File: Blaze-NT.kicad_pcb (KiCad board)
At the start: 2 copper layers, 44.4 x 44.7 mm, 67 parts, among them J1 Micro_SD_Card, J2 TC2030-NL, J3 USB_C_Receptacle, J4 ARM, J5 BATTERY, SW1 SW_SPST, SW2 SW_SPST, U1 W25Q128JVS, U2 STM32F411CEUx, U3 USBLC6-2SC6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

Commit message: Silk updates
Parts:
- added J6: Stemma, Connector_JST:JST_SH_SM04B-SRSS-TB_1x04-1MP_P1.00mm_Horizontal, F.Cu at (130.7, 114.2)
- added R16: 5.1k, Resistor_SMD:R_0603_1608Metric, F.Cu at (134.8, 112.7)
- added R17: 5.1k, Resistor_SMD:R_0603_1608Metric, F.Cu at (134.8, 115.7)
- moved SW2 44.7 mm to (147.2, 92.9)
- moved H4 43.1 mm to (131.0, 121.6)
- moved C2 43.1 mm to (150.3, 105.8)
- moved C3 43.1 mm to (148.7, 105.8)
- moved C6 43.1 mm to (142.6, 94.7)
- moved H1 43.1 mm to (131.0, 84.0)
- moved U4 43.1 mm to (149.5, 119.3)
- moved Y2 43.1 mm to (144.9, 105.6)
- moved AE1 43.1 mm to (156.4, 123.1)
- moved C10 43.1 mm to (159.4, 97.2)
- moved C11 43.1 mm to (157.9, 97.2)
- moved C12 43.1 mm to (152.5, 98.0)
- moved C15 43.1 mm to (163.7, 120.3)
- moved C16 43.1 mm to (162.2, 120.3)
- moved C24 43.1 mm to (152.5, 99.5)
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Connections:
- U2 pad 42: unconnected-(U2-PB6-Pad42) -> /Microcontroller/SCL
- U2 pad 43: unconnected-(U2-PB7-Pad43) -> /Microcontroller/SDA
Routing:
- net /Microcontroller/SCL: track 0.00 -> 27.3 mm, vias 0 -> 2
- net /Microcontroller/SDA: track 0.00 -> 26.9 mm, vias 0 -> 2
- net /Microcontroller/BOOT0: track 25.7 -> 14.9 mm, vias 0 -> 3
- net +5V: track 52.9 -> 57.7 mm
- net /Microcontroller/nRST: track 50.0 -> 53.4 mm
- net /Power Managment/VBATT_Sense/VBATT_IN: track 5.76 -> 7.92 mm
- net +3V3: track 194.5 -> 196.3 mm, vias 5 -> 6
- net Net-(J4-Pin_1): track 34.0 -> 35.5 mm
- net GND: track 0.00 -> 1.46 mm, vias 0 -> 64
- net /Microcontroller/SWD: track 19.8 -> 19.0 mm
- net Net-(D3-A): track 18.2 -> 17.5 mm
- net /MISO: track 108.6 -> 109.3 mm
- net /MOSI: track 111.6 -> 111.0 mm
- net Net-(U4-SW-Pad4): vias 0 -> 7
- net (no net): vias 0 -> 1
- added copper zone on B.Cu, net Net-(U4-SW-Pad4)

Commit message: Addeed part numbers
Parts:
- added D5: LED, LED_SMD:LED_0603_1608Metric, F.Cu at (145.9, 114.5)
- added G***: LOGO, Avionics_Feet:Mermaid-Cat, F.Cu at (163.0, 110.4)
- added R18: 120, Resistor_SMD:R_0603_1608Metric, F.Cu at (142.7, 114.5)
- Y2: footprint Oscillator:Oscillator_SMD_Abracon_ASCO-4Pin_1.6x1.2mm -> Avionics_Feet:OSC_SIT1532AI-J4-DCC-32.768D
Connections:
- Y2 pad 1: +3V3 -> GND
- Y2 pad 2: GND -> /Microcontroller/LSE_IN
- Y2 pad 3: /Microcontroller/LSE_IN -> +3V3
- Y2 pad 4: +3V3 -> GND
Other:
- board text added: "+"
- board text added: "-"
- board text added: "2026"
- board text added: "4.5V - 21V 3W"
- board text added: "50Ω"
- board text added: "::<>"
- board text added: "ARM"
- board text added: "BATTERY"
- board text added: "BLAZE NT"
- board text added: "BOOT0"
- board text added: "RESET"
- board text added: "SCL SDA 3V3 GND"
- board text added: "STEMMA"
- board text added: "UCSC"

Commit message: Added prod files
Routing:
- net +3V3: track 195.8 -> 198.1 mm
- net /Microcontroller/SWD: track 19.0 -> 19.6 mm
- net GND: vias 64 -> 74
- net (no net): vias 1 -> 0
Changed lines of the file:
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@@
 		)
 	)
-	(via
-		(at 144.9832 107.0102)
-		(size 0.4)
-		(drill 0.2)
-		(layers "F.Cu" "B.Cu")
-		(net 0)
-	)
 	(segment
 		(start 149.248 120.549)
@@
 	)
 	(via
+		(at 144.272 110.744)
+		(size 0.4)
+		(drill 0.2)
+		(layers "F.Cu" "B.Cu")
+		(free yes)
+		(net 1)
+	)
+	(via
 		(at 152.546 97.197)
 		(size 0.4)
@@
 	)
 	(via
+		(at 165.354 103.251)
+		(size 0.4)
+		(drill 0.2)
+		(layers "F.Cu" "B.Cu")
+		(free yes)
+		(net 1)
+	)
+	(via
 		(at 155.34 115.231)
 		(size 0.4)
@@
 	)
 	(via
+		(at 144.653 113.03)
+		(size 0.4)
+		(drill 0.2)
+		(layers "F.Cu" "B.Cu")
+		(free yes)
+		(net 1)
+	)
+	(via
+		(at 159.131 92.71)
+		(size 0.4)
+		(drill 0.2)
+		(layers "F.Cu" "B.Cu")
+		(free yes)
+		(net 1)
+	)
+	(via
 		(at 157.118 114.723)
 		(size 0.4)
@@
 	)
 	(via
+		(at 146.177 116.205)
+		(size 0.4)
+		(drill 0.2)
+		(layers "F.Cu" "B.Cu")
+		(free yes)
+		(net 1)
+	)
+	(via
 		(at 155.594 120.311)
 		(size 0.4)
@@
 	)
 	(via
+		(at 141.097 113.03)
+		(size 0.4)
+		(drill 0.2)
+		(layers "F.Cu" "B.Cu")
+		(free yes)
+		(net 1)
+	)
+	(via
 		(at 155.594 118.787)
 		(size 0.4)
@@
 	)
 	(via
+		(at 147.447 107.442)
+		(size 0.4)
+		(drill 0.2)
+		(layers "F.Cu" "B.Cu")
+		(free yes)
+		(net 1)
+	)
+	(via
 		(at 155.34 117.771)
 		(size 0.4)
@@
 	)
 	(via
+		(at 144.145 109.347)
+		(size 0.4)
+		(drill 0.2)
+		(layers "F.Cu" "B.Cu")
+		(free yes)
+		(net 1)
+	)
+	(via
 		(at 147.447 117.729)
 		(size 0.4)
@@
 	)
 	(via
+		(at 145.034 107.315)
+		(size 0.4)
+		(drill 0.2)
+		(layers "F.Cu" "B.Cu")
+		(free yes)
+		(net 1)
+	)
+	(via
 		(at 155.594 118.279)
 		(size 0.4)
@@
 	)
 	(via
-		(at 155.594 92.752)
+		(at 155.575 92.71)
 		(size 0.4)
 		(drill 0.2)
@@
 	)
 	(via
-		(at 157.118 92.752)
+		(at 157.099 92.71)
 		(size 0.4)
 		(drill 0.2)
@@
 		(net 1)
 	)
+	(via
+		(at 165.354 105.029)
+		(size 0.4)
+		(drill 0.2)
+		(layers "F.Cu" "B.Cu")
+		(free yes)
+		(net 1)
+	)
 	(segment
 		(start 156.356 116.501)
@@
 	)
 	(segment
+		(start 148.482 113.186)
+		(end 148.18 113.186)
+		(width 0.254)
+		(layer "F.Cu")
+		(net 3)
+	)
+	(segment
 		(start 148.545 123.93)
 		(end 149.37 123.105)
@@
 	)
 	(segment
+		(start 146.8882 114.4778)
+		(end 146.7105 114.4778)
+		(width 0.254)
+		(layer "F.Cu")
+		(net 3)
+	)
+	(segment
 		(start 147.954 103.4285)
 		(end 147.954 104.276)
@@
 	)
 	(segment
+		(start 148.18 113.186)
+		(end 146.8882 114.4778)
+		(width 0.254)
+		(layer "F.Cu")
+		(net 3)
+	)
+	(segment
 		(start 146.4815 108.754)
 		(end 148.342 108.754)
@@
 	(segment
 		(start 143.5274 96.8144)
-		(end 143.5274 100.6244)
+		(end 145.669 98.956)
 		(width 0.254)
 		(layer "B.Cu")
@@
 	)
 	(segment
-		(start 143.5274 100.6244)
+		(start 145.669 98.956)
+		(end 145.669 102.766)
+		(width 0.254)
+		(layer "B.Cu")
+		(net 4)
+	)
+	(segment
+		(start 145.669 102.766)
 		(end 146.958 104.055)
 		(width 0.254)
@@
 	)
 	(segment
-		(start 145.434 95.419)
-		(end 159.404 95.419)
+		(start 144.926 95.927)
+		(end 145.857 94.996)
 		(width 0.254)
 		(layer "B.Cu")
@@
 	)
 	(segment
-		(start 159.404 95.419)
+		(start 159.0716 95.0866)
 		(end 160.674 96.689)
 		(width 0.254)
@@
 	)
 	(segment
-		(start 144.926 95.927)
-		(end 145.434 95.419)
+		(start 158.2124 94.996)
+		(end 158.2124 95.088947)
+		(width 0.254)
+		(layer "B.Cu")
+		(net 24)
+	)
+	(segment
+		(start 158.2124 95.088947)
+		(end 158.464053 95.3406)
+		(width 0.254)
+		(layer "B.Cu")
+		(net 24)
+	)
+	(segment
+		(start 158.464053 95.3406)
+		(end 158.819947 95.3406)
+		(width 0.254)
+		(layer "B.Cu")
+		(net 24)
+	)
+	(segment
+		(start 159.0716 95.088947)
+		(end 159.0716 95.0866)
+		(width 0.254)
+		(layer "B.Cu")
+		(net 24)
+	)
+	(segment
+		(start 145.857 94.996)
+		(end 158.2124 94.996)
+		(width 0.254)
+		(layer "B.Cu")
+		(net 24)
+	)
+	(segment
+		(start 158.819947 95.3406)
+		(end 159.0716 95.088947)
 		(width 0.254)
 		(layer "B.Cu")
@@
 	)
 	(segment
-		(start 142.596 96.479)
-		(end 142.596 97.241)
+		(start 144.968 94.107)
+		(end 142.596 96.479)
 		(width 0.254)
 		(layer "B.Cu")
@@
 	)
 	(segment
-		(start 144.672 94.403)
-		(end 142.596 96.479)
+		(start 142.596 96.479)
+		(end 142.596 97.241)
 		(width 0.254)
 		(layer "B.Cu")
@@
 	)
 	(segment
-		(start 158.134 94.403)
-		(end 144.672 94.403)
+		(start 157.838 94.107)
+		(end 144.968 94.107)
 		(width 0.254)
 		(layer "B.Cu")
@@
 	(segment
 		(start 158.642 94.911)
-		(end 158.134 94.403)
+		(end 157.838 94.107)
 		(width 0.254)
 		(layer "B.Cu")
@@
 	)
 	(segment
+		(start 146.7146 94.579)
+		(end 147.212 94.579)
+		(width 0.254)
+		(layer "F.Cu")
+		(net 31)
+	)
+	(segment
+		(start 146.671199 94.535599)
+		(end 146.7146 94.579)
+		(width 0.254)
+		(layer "F.Cu")
+		(net 31)
+	)
+	(segment
 		(start 143.2665 100.741)
 		(end 142.5726 100.741)
@@
 	)
 	(segment
-		(start 146.3826 94.911)
-		(end 146.7146 94.579)
+		(start 142.135692 92.625)
+		(end 143.405692 93.895)
 		(width 0.254)
 		(layer "F.Cu")
@@
 	)
 	(segment
-		(start 142.135692 92.625)
-		(end 143.405692 93.895)
+		(start 146.361311 94.535599)
+		(end 146.671199 94.535599)
 		(width 0.254)
 		(layer "F.Cu")
@@
 	)
 	(segment
-		(start 146.7146 94.579)
-		(end 147.212 94.579)
-		(width 0.254)
-		(layer "F.Cu")
-		(net 31)
-	)
-	(segment
 		(start 143.777136 93.895)
 		(end 144.3826 94.500464)
@@
 	)
 	(via
-		(at 146.3826 94.911)
+		(at 146.361311 94.535599)
 		(size 0.4)
 		(drill 0.2)
@@
 	)
 	(segment
-		(start 146.3826 94.911)
-		(end 144.823253 94.911)
+		(start 146.361311 94.535599)
+		(end 145.198654 94.535599)
 		(width 0.254)
 		(layer "B.Cu")
@@
 	)
 	(segment
-		(start 143.0978 100.2158)
-		(end 142.5606 100.753)
+		(start 145.198654 94.535599)
+		(end 143.0978 96.636453)
 		(width 0.254)
 		(layer "B.Cu")
@@
 	)
 	(segment
-		(start 143.0978 96.636453)
-		(end 143.0978 100.2158)
+		(start 143.0978 100.2158)
+		(end 142.5606 100.753)
 		(width 0.254)
 		(layer "B.Cu")
@@
 	)
 	(segment
-		(start 144.823253 94.911)
-		(end 143.0978 96.636453)
+		(start 143.0978 96.636453)
+		(end 143.0978 100.2158)
 		(width 0.254)
 		(layer "B.Cu")

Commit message: Silk updates
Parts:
- added G***: LOGO, Avionics_Feet:Blaze, B.Cu at (161.4, 99.9)
- added G***: LOGO, Avionics_Feet:Emi, B.Cu at (136.9, 113.3)
- added REF**: Smolhaj_Scale_0.1, Symbol:Smolhaj_Scale_0.1, B.Cu at (120.5, 89.9)
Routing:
- net Net-(D5-K): track 0.00 -> 1.57 mm
- net +5V: track 57.7 -> 58.9 mm
- net /Microcontroller/BOOT0: track 14.9 -> 15.6 mm
- net /Microcontroller/SWD: track 19.6 -> 20.3 mm
- net /Microcontroller/nRST: track 53.4 -> 53.9 mm
- net Net-(J4-Pin_1): track 35.5 -> 36.0 mm
- net GND: vias 74 -> 76
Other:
- board text added: "'><'"
- board text added: "._./"
- board text added: "O_•^"
- board text added: "^ω^~"

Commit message: PCB revisions
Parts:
- removed REF**: Smolhaj_Scale_0.1, Symbol:Smolhaj_Scale_0.1
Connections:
- U2 pad 10: /Microcontroller/CS_IMU_AG -> /CS_POWER
- U2 pad 11: /Microcontroller/CS_IMU_MAG -> /Microcontroller/CS_IMU_AG
- U2 pad 12: /CS_POWER -> /Microcontroller/CS_IMU_MAG
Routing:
- net /CS_POWER: track 27.1 -> 23.5 mm
- net +3V3: track 198.0 -> 195.4 mm
- net /MOSI: track 110.8 -> 108.4 mm
- net /MISO: track 109.3 -> 107.5 mm
- net /Microcontroller/LED_BLUE: track 36.3 -> 37.9 mm
- net /Microcontroller/LED_GREEN: track 37.6 -> 39.2 mm
- net /Microcontroller/LED_RED: track 39.4 -> 40.8 mm
- net +5V: track 58.9 -> 60.1 mm
- net /SCK: track 103.1 -> 102.0 mm
- net Net-(U9-IN+): track 6.68 -> 7.54 mm
- net unconnected-(U2-PB12-Pad25): track 0.64 -> 0.00 mm
- net /Microcontroller/CS_IMU_MAG: track 16.8 -> 17.4 mm
- net /Microcontroller/CS_IMU_AG: track 17.6 -> 18.1 mm
- net /Microcontroller/BOOT0: track 15.6 -> 15.1 mm
- net /RST_RADIO: track 12.4 -> 11.9 mm
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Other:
- board text added: "<3"

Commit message: Added fiducials
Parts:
- added FID1: Fiducial, Avionics_Feet:JLC_Fiducial, F.Cu at (133.9, 86.6)
- added FID2: Fiducial, Avionics_Feet:JLC_Fiducial, F.Cu at (134.1, 119.4)
- added FID3: Fiducial, Avionics_Feet:JLC_Fiducial, F.Cu at (165.4, 86.9)
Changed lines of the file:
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@@
 		)
 	)
+	(footprint "Avionics_Feet:JLC_Fiducial"
+		(layer "F.Cu")
+		(at 134.112 119.38)
+		(property "Reference" "FID2"
+			(at 0 -0.5 0)
+			(unlocked yes)
+			(layer "F.SilkS")
+			(hide yes)
+			(effects
+				(font
+					(size 1 1)
+					(thickness 0.1)
+				)
+			)
+		)
+		(property "Value" "Fiducial"
+			(at 0 1 0)
+			(unlocked yes)
+			(layer "F.Fab")
+			(effects
+				(font
+					(size 1 1)
+					(thickness 0.15)
+				)
+			)
+		)
+		(property "Datasheet" "~"
+			(at 0 0 0)
+			(unlocked yes)
+			(layer "F.Fab")
+			(hide yes)
+			(effects
+				(font
+					(size 1 1)
+					(thickness 0.15)
+				)
+			)
+		)
+		(property "Description" "Fiducial Marker"
+			(at 0 0 0)
+			(unlocked yes)
+			(layer "F.Fab")
+			(hide yes)
+			(effects
+				(font
+					(size 1 1)
+					(thickness 0.15)
+				)
+			)
+		)
+		(property ki_fp_filters "Fiducial*")
+		(sheetname "/")
+		(sheetfile "Blaze-NT.kicad_sch")
+		(attr smd exclude_from_bom dnp)
+		(fp_text user "${REFERENCE}"
+			(at 0 2.5 0)
+			(unlocked yes)
+			(layer "F.Fab")
+			(effects
+				(font
+					(size 1 1)
+					(thickness 0.15)
+				)
+			)
+		)
+		(pad "" np_thru_hole circle
+			(at 0 0)
+			(size 1.4478 1.4478)
+			(drill 1.15316)
+			(layers "*.Cu" "*.Mask")
+		)
+		(embedded_fonts no)
+	)
+	(footprint "Avionics_Feet:JLC_Fiducial"
+		(layer "F.Cu")
+		(at 133.858 86.614)
+		(property "Reference" "FID1"
+			(at 0 -0.5 0)
+			(unlocked yes)
+			(layer "F.SilkS")
+			(hide yes)
+			(effects
+				(font
+					(size 1 1)
+					(thickness 0.1)
+				)
+			)
+		)
+		(property "Value" "Fiducial"
+			(at 0 1 0)
+			(unlocked yes)
+			(layer "F.Fab")
+			(effects
+				(font
+					(size 1 1)
+					(thickness 0.15)
+				)
+			)
+		)
+		(property "Datasheet" "~"
+			(at 0 0 0)
+			(unlocked yes)
+			(layer "F.Fab")
+			(hide yes)
+			(effects
+				(font
+					(size 1 1)
+					(thickness 0.15)
+				)
+			)
+		)
+		(property "Description" "Fiducial Marker"
+			(at 0 0 0)
+			(unlocked yes)
+			(layer "F.Fab")
+			(hide yes)
+			(effects
+				(font
+					(size 1 1)
+					(thickness 0.15)
+				)
+			)
+		)
+		(property ki_fp_filters "Fiducial*")
+		(sheetname "/")
+		(sheetfile "Blaze-NT.kicad_sch")
+		(attr smd exclude_from_bom dnp)
+		(fp_text user "${REFERENCE}"
+			(at 0 2.5 0)
+			(unlocked yes)
+			(layer "F.Fab")
+			(effects
+				(font
+					(size 1 1)
+					(thickness 0.15)
+				)
+			)
+		)
+		(pad "" np_thru_hole circle
+			(at 0 0)
+			(size 1.4478 1.4478)
+			(drill 1.15316)
+			(layers "*.Cu" "*.Mask")
+		)
+		(embedded_fonts no)
+	)
 	(footprint "Resistor_SMD:R_0603_1608Metric"
 		(layer "F.Cu")
@@
 		)
 	)
+	(footprint "Avionics_Feet:JLC_Fiducial"
+		(layer "F.Cu")
+		(at 165.354 86.868)
+		(property "Reference" "FID3"
+			(at 0 -0.5 0)
+			(unlocked yes)
+			(layer "F.SilkS")
+			(hide yes)
+			(effects
+				(font
+					(size 1 1)
+					(thickness 0.1)
+				)
+			)
+		)
+		(property "Value" "Fiducial"
+			(at 0 1 0)
+			(unlocked yes)
+			(layer "F.Fab")
+			(effects
+				(font
+					(size 1 1)
+					(thickness 0.15)
+				)
+			)
+		)
+		(property "Datasheet" "~"
+			(at 0 0 0)
+			(unlocked yes)
+			(layer "F.Fab")
+			(hide yes)
+			(effects
+				(font
+					(size 1 1)
+					(thickness 0.15)
+				)
+			)
+		)
+		(property "Description" "Fiducial Marker"
+			(at 0 0 0)
+			(unlocked yes)
+			(layer "F.Fab")
+			(hide yes)
+			(effects
+				(font
+					(size 1 1)
+					(thickness 0.15)
+				)
+			)
+		)
+		(property ki_fp_filters "Fiducial*")
+		(sheetname "/")
+		(sheetfile "Blaze-NT.kicad_sch")
+		(attr smd exclude_from_bom dnp)
+		(fp_text user "${REFERENCE}"
+			(at 0 2.5 0)
+			(unlocked yes)
+			(layer "F.Fab")
+			(effects
+				(font
+					(size 1 1)
+					(thickness 0.15)
+				)
+			)
+		)
+		(pad "" np_thru_hole circle
+			(at 0 0)
+			(size 1.4478 1.4478)
+			(drill 1.15316)
+			(layers "*.Cu" "*.Mask")
+		)
+		(embedded_fonts no)
+	)
 	(footprint "Capacitor_SMD:C_0603_1608Metric"

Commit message: Added Digikey Components
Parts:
- Y2: value 32.768KHz -> 32.768kHz; footprint Avionics_Feet:OSC_SIT1532AI-J4-DCC-32.768D -> Oscillator:Oscillator_SMD_Abracon_ASCO-4Pin_1.6x1.2mm
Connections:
- Y2 pad 1: GND -> +3V3
- Y2 pad 2: /Microcontroller/LSE_IN -> GND
- Y2 pad 3: +3V3 -> /Microcontroller/LSE_IN
- Y2 pad 4: GND -> +3V3
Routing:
- net +3V3: track 195.4 -> 191.4 mm
- net /INT_RADIO: track 26.5 -> 28.5 mm
- net +5V: track 60.1 -> 61.0 mm, vias 2 -> 3

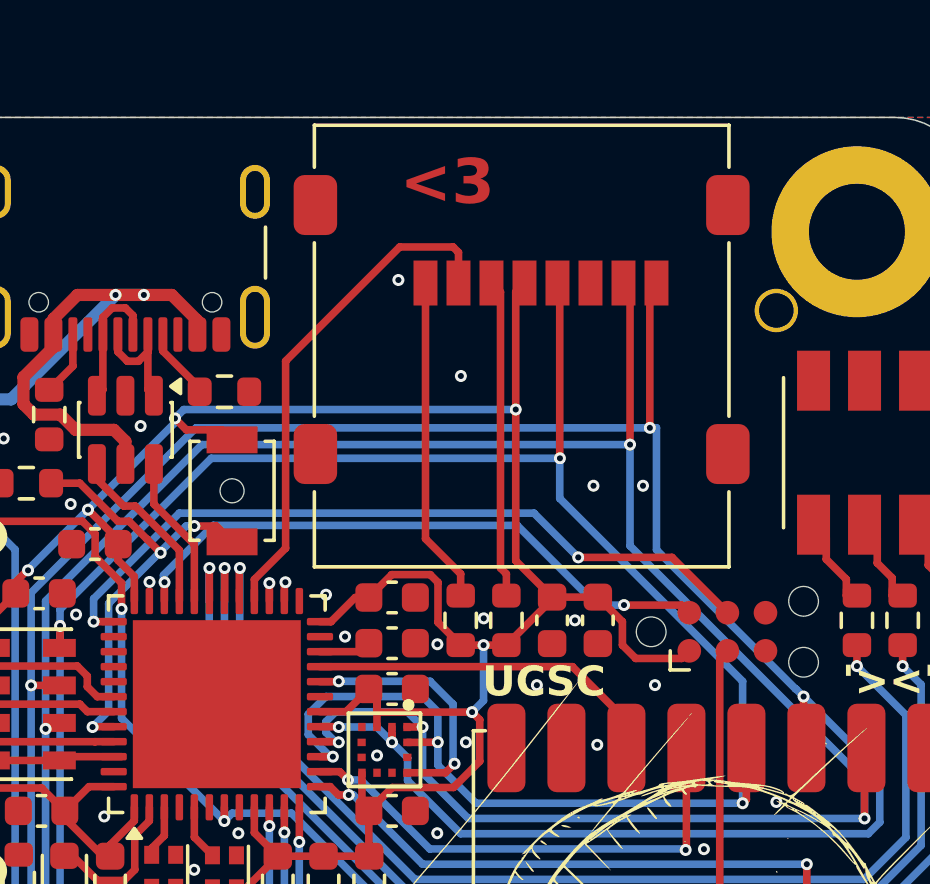
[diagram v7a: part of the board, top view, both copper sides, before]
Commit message: Updated SD card to corrected symbol
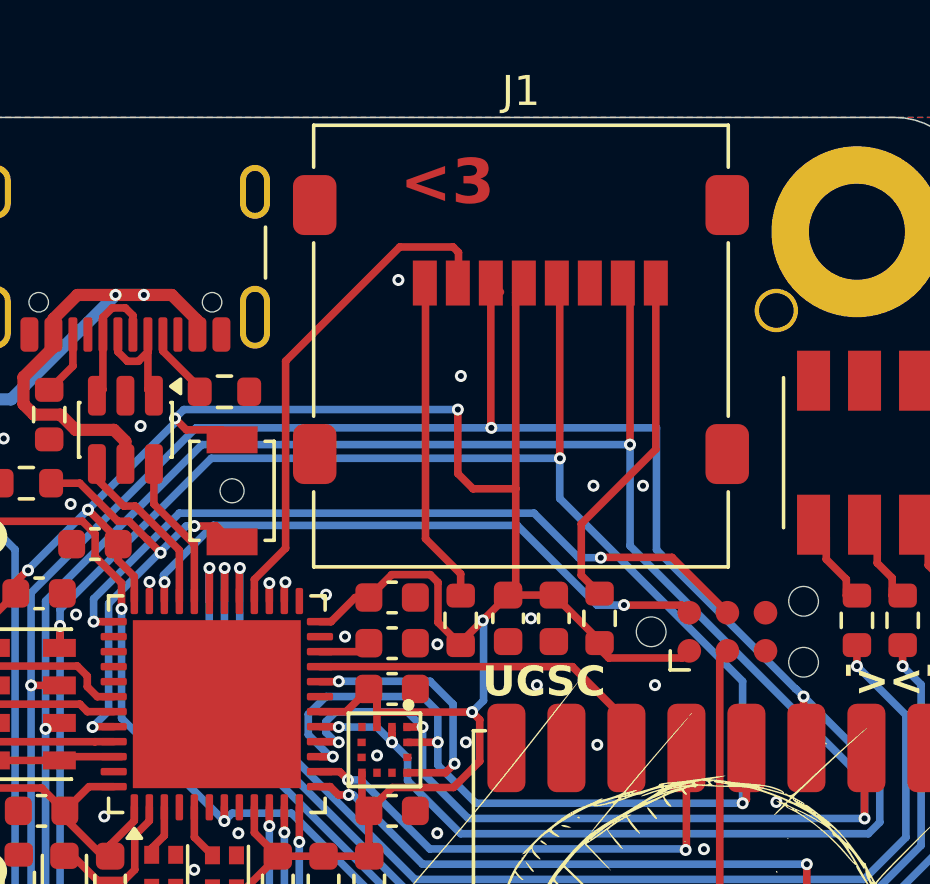
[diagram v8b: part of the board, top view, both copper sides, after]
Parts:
- moved R2 3.11 mm to (159.5, 97.1)
- moved C10 1.47 mm to (157.9, 97.1)
- moved C11 1.47 mm to (156.4, 97.1)
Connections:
- J1 pad 3: Net-(J1-CMD) -> /MOSI
- J1 pad 8: /MOSI -> Net-(J1-DAT1)
- R2 pad 1: Net-(J1-CMD) -> Net-(J1-DAT1)
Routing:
- net Net-(J1-DAT1): track 0.00 -> 11.9 mm
- net Net-(J1-CMD): track 10.6 -> 0.00 mm
- net +3V3: track 191.4 -> 193.9 mm
- net GND: vias 91 -> 90
